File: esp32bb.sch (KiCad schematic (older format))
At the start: 31 parts, among them CON1 Micro_SD_Card, IC1 FT232RQ, P1 CONN_01X17, P2 CONN_01X17, P3 USB_OTG, Q1 MMBT3904, Q2 MMBT3904, SW1 SWITCH_SPST, SW2 SWITCH_SPST, U1 ESP32-WROOM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

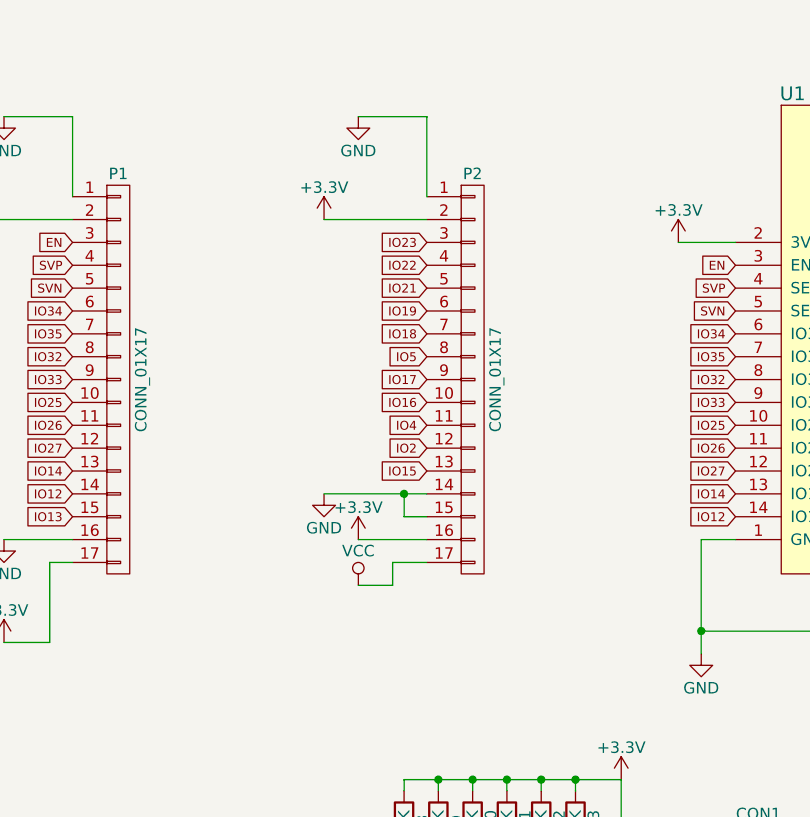
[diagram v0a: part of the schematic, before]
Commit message: Add RX TX to headers
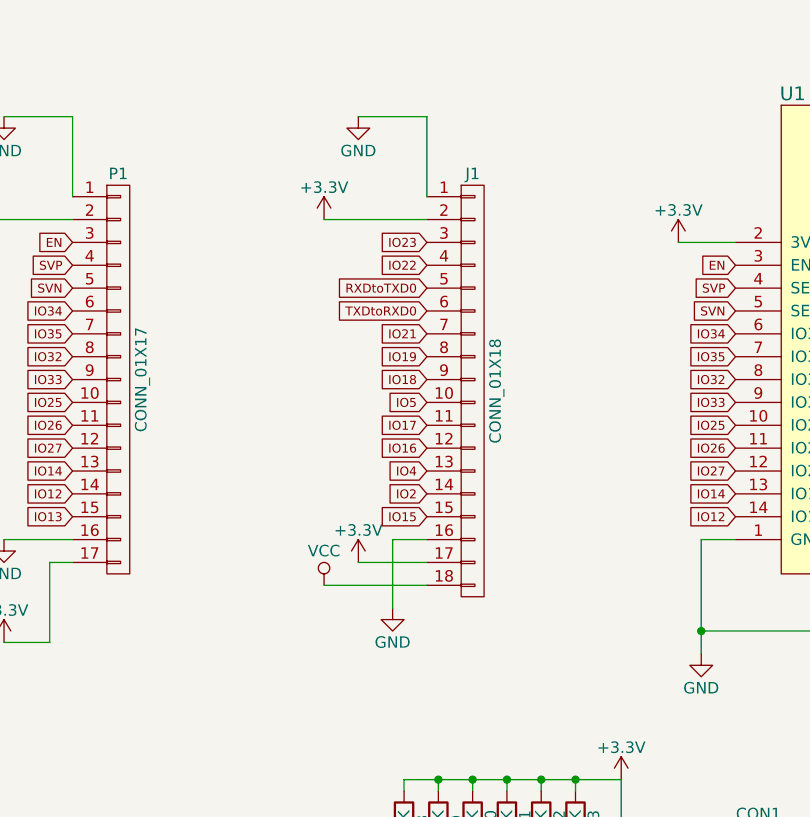
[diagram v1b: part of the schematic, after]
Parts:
- removed P2: CONN_01X17, Pin_Headers:Pin_Header_Straight_1x17_Pitch2.54mm, symbol CONN_01X17
- added J1: CONN_01X18, common:Pin_Header_Straight_1x18_Pitch2.54mm, symbol CONN_01X18
- P1: footprint Pin_Headers:Pin_Header_Straight_1x17_Pitch2.54mm -> common:Pin_Header_Straight_1x17_Pitch2.54mm
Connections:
- net +3V3: now also J1.17 (P17), J1.2 (P2)
- net GND: now also J1.1 (P1), J1.16 (P16)
- net IO15: now also J1.15 (P15)
- net IO16: now also J1.12 (P12)
- net IO17: now also J1.11 (P11)
- net IO18: now also J1.9 (P9)
- net IO19: now also J1.8 (P8)
- net IO2: now also J1.14 (P14)
- net IO21: now also J1.7 (P7)
- net IO22: now also J1.4 (P4)
- net IO23: now also J1.3 (P3)
- net IO4: now also J1.13 (P13)
- net IO5: now also J1.10 (P10)
- net RXDtoTXD0: now also J1.5 (P5)
- net TXDtoRXD0: now also J1.6 (P6)
- net VCC: now also J1.18 (P18)
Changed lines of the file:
@@
 Text GLabel 3200 3250 0    39   Input ~ 0
 IO22
-Text GLabel 3200 3350 0    39   Input ~ 0
+Text GLabel 3200 3550 0    39   Input ~ 0
 IO21
-Text GLabel 3200 3450 0    39   Input ~ 0
+Text GLabel 3200 3650 0    39   Input ~ 0
 IO19
-Text GLabel 3200 3550 0    39   Input ~ 0
+Text GLabel 3200 3750 0    39   Input ~ 0
 IO18
-Text GLabel 3200 3650 0    39   Input ~ 0
+Text GLabel 3200 3850 0    39   Input ~ 0
 IO5
-Text GLabel 3200 3750 0    39   Input ~ 0
+Text GLabel 3200 3950 0    39   Input ~ 0
 IO17
-Text GLabel 3200 3850 0    39   Input ~ 0
+Text GLabel 3200 4050 0    39   Input ~ 0
 IO16
-Text GLabel 3200 3950 0    39   Input ~ 0
+Text GLabel 3200 4150 0    39   Input ~ 0
 IO4
-Text GLabel 3200 4050 0    39   Input ~ 0
+Text GLabel 3200 4250 0    39   Input ~ 0
 IO2
-Text GLabel 3200 4150 0    39   Input ~ 0
+Text GLabel 3200 4350 0    39   Input ~ 0
 IO15
 $Comp
@@
 L VCC #PWR015
 U 1 1 58948CFD
-P 2900 4650
-F 0 "#PWR015" H 2900 4500 50  0001 C CNN
-F 1 "VCC" H 2900 4800 50  0000 C CNN
-F 2 "" H 2900 4650 50  0000 C CNN
-F 3 "" H 2900 4650 50  0000 C CNN
-	1    2900 4650
+P 2750 4650
+F 0 "#PWR015" H 2750 4500 50  0001 C CNN
+F 1 "VCC" H 2750 4800 50  0000 C CNN
+F 2 "" H 2750 4650 50  0000 C CNN
+F 3 "" H 2750 4650 50  0000 C CNN
+	1    2750 4650
 	1    0    0    -1
 $EndComp
@@
 L +3.3V #PWR016
 U 1 1 58948D8F
-P 2900 4450
-F 0 "#PWR016" H 2900 4300 50  0001 C CNN
-F 1 "+3.3V" H 2900 4590 50  0000 C CNN
-F 2 "" H 2900 4450 50  0000 C CNN
-F 3 "" H 2900 4450 50  0000 C CNN
-	1    2900 4450
+P 2900 4550
+F 0 "#PWR016" H 2900 4400 50  0001 C CNN
+F 1 "+3.3V" H 2900 4690 50  0000 C CNN
+F 2 "" H 2900 4550 50  0000 C CNN
+F 3 "" H 2900 4550 50  0000 C CNN
+	1    2900 4550
 	1    0    0    -1
 $EndComp
@@
 L GND #PWR019
 U 1 1 58948FCD
-P 2750 4250
-F 0 "#PWR019" H 2750 4000 50  0001 C CNN
-F 1 "GND" H 2750 4100 50  0000 C CNN
-F 2 "" H 2750 4250 50  0000 C CNN
-F 3 "" H 2750 4250 50  0000 C CNN
-	1    2750 4250
+P 3050 4750
+F 0 "#PWR019" H 3050 4500 50  0001 C CNN
+F 1 "GND" H 3050 4600 50  0000 C CNN
+F 2 "" H 3050 4750 50  0000 C CNN
+F 3 "" H 3050 4750 50  0000 C CNN
+	1    3050 4750
 	1    0    0    -1
 $EndComp
@@
 F 0 "P1" H 1850 4650 50  0000 C CNN
 F 1 "CONN_01X17" V 1950 3750 50  0000 C CNN
-F 2 "Pin_Headers:Pin_Header_Straight_1x17_Pitch2.54mm" H 1850 3750 50  0001 C CNN
+F 2 "common:Pin_Header_Straight_1x17_Pitch2.54mm" H 1850 3750 50  0001 C CNN
 F 3 "" H 1850 3750 50  0000 C CNN
 	1    1850 3750
-	1    0    0    -1
-$EndComp
-$Comp
-L CONN_01X17 P2
-U 1 1 58A7A491
-P 3400 3750
-F 0 "P2" H 3400 4650 50  0000 C CNN
-F 1 "CONN_01X17" V 3500 3750 50  0000 C CNN
-F 2 "Pin_Headers:Pin_Header_Straight_1x17_Pitch2.54mm" H 3400 3750 50  0001 C CNN
-F 3 "" H 3400 3750 50  0000 C CNN
-	1    3400 3750
 	1    0    0    -1
 $EndComp
@@
 	1    0    0    -1
 $EndComp
+$Comp
+L CONN_01X18 J1
+U 1 1 58B95980
+P 3400 3800
+F 0 "J1" H 3400 4750 50  0000 C CNN
+F 1 "CONN_01X18" V 3500 3800 50  0000 C CNN
+F 2 "common:Pin_Header_Straight_1x18_Pitch2.54mm" H 3400 3800 50  0001 C CNN
+F 3 "" H 3400 3800 50  0001 C CNN
+	1    3400 3800
+	1    0    0    -1
+$EndComp
 Wire Wire Line
 	4300 3150 4550 3150
@@
 	3200 2600 3200 2950
 Wire Wire Line
-	2900 4450 3200 4450
+	2900 4550 3200 4550
 Wire Wire Line
 	1350 4450 1650 4450
-Wire Wire Line
-	2750 4250 3200 4250
-Wire Wire Line
-	3100 4250 3100 4350
-Wire Wire Line
-	3100 4350 3200 4350
-Connection ~ 3100 4250
 Wire Wire Line
 	7400 2900 7700 2900
@@
 Wire Wire Line
 	1550 4900 1350 4900
-Wire Wire Line
-	2900 4650 3050 4650
-Wire Wire Line
-	3050 4650 3050 4550
-Wire Wire Line
-	3050 4550 3200 4550
 Wire Wire Line
 	9800 5550 9800 5650
@@
 	3100 5850 3100 6650
 Connection ~ 3100 6650
+Wire Wire Line
+	2750 4650 3200 4650
+Wire Wire Line
+	3050 4750 3050 4450
+Wire Wire Line
+	3050 4450 3200 4450
+Text GLabel 3200 3350 0    39   Input ~ 0
+RXDtoTXD0
+Text GLabel 3200 3450 0    39   Input ~ 0
+TXDtoRXD0
 $EndSCHEMATC

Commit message: Show component number on fab layer
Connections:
- net GND: now also D2.1 (K); no longer R7.2
- net IO2: now also R7.1; no longer D2.2 (A)
- new net: D2.2 (A), R7.2
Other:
- moved on the sheet: D2, R7
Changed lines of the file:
@@
 Sheet 1 1
 Title "ESP32BB"
-Date "2017-03-02"
-Rev "1.2"
+Date "2017-03-04"
+Rev "1.3"
 Comp ""
 Comment1 "by asukiaaa"
@@
 L LED D2
 U 1 1 58AAE67A
-P 7350 1450
-F 0 "D2" H 7350 1550 50  0000 C CNN
-F 1 "D02" H 7350 1350 50  0000 C CNN
-F 2 "LEDs:LED_0603" H 7350 1450 50  0001 C CNN
-F 3 "" H 7350 1450 50  0000 C CNN
-	1    7350 1450
+P 7650 1450
+F 0 "D2" H 7650 1550 50  0000 C CNN
+F 1 "D02" H 7650 1350 50  0000 C CNN
+F 2 "LEDs:LED_0603" H 7650 1450 50  0001 C CNN
+F 3 "" H 7650 1450 50  0000 C CNN
+	1    7650 1450
 	-1   0    0    1
 $EndComp
@@
 L R R7
 U 1 1 58AAF2B1
-P 7650 1450
-F 0 "R7" V 7730 1450 50  0000 C CNN
-F 1 "10K" V 7650 1450 50  0000 C CNN
-F 2 "Resistors_SMD:R_0603" V 7580 1450 50  0001 C CNN
-F 3 "" H 7650 1450 50  0000 C CNN
-	1    7650 1450
+P 7350 1450
+F 0 "R7" V 7430 1450 50  0000 C CNN
+F 1 "10K" V 7350 1450 50  0000 C CNN
+F 2 "Resistors_SMD:R_0603" V 7280 1450 50  0001 C CNN
+F 3 "" H 7350 1450 50  0000 C CNN
+	1    7350 1450
 	0    -1   -1   0
 $EndComp
